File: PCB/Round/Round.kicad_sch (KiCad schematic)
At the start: 50 parts, among them J3 Conn, SW1 ESE13V01D, U1 PN532, U2 QR, Y1 27.12MHz

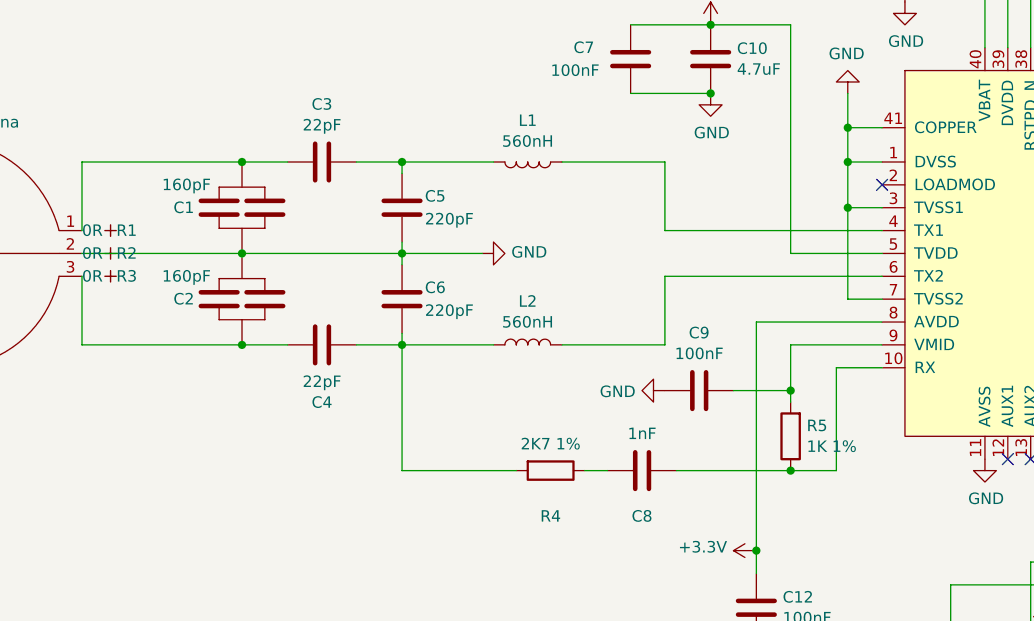
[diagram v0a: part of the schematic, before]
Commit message: Production nearly ready - may have to change to square LEDs.
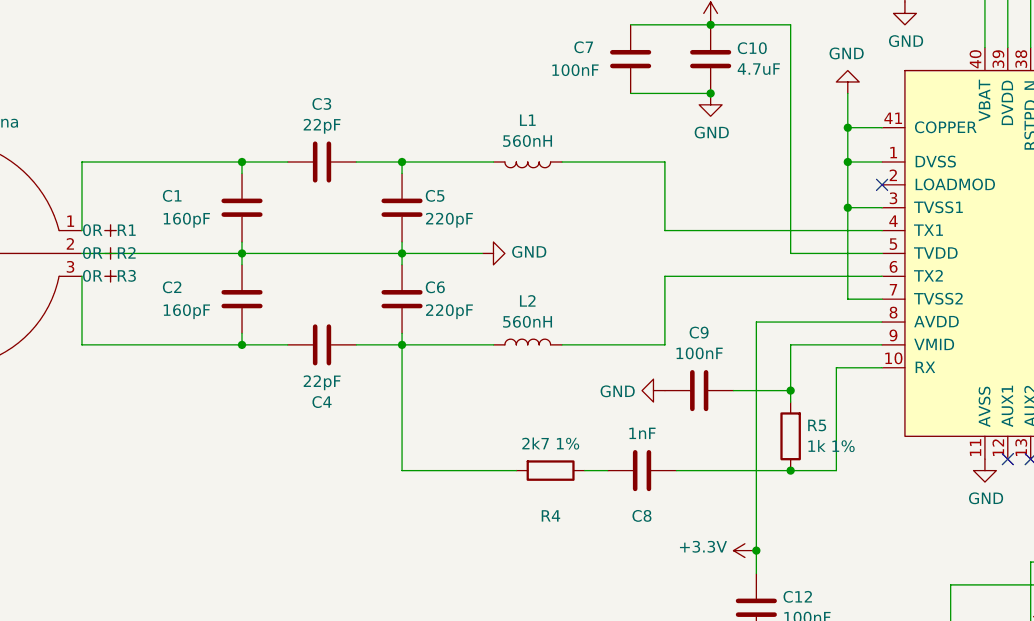
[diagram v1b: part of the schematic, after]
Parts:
- removed C1, C2: 160pF, RevK:C_0603, symbol RevK:Cx2
- added C1, C2: 160pF, RevK:C_0603, symbol Device:C
- D1: JLCPCB Rotation Offset (none) -> 180; LCSC Part # (none) -> C4749157
- D2: JLCPCB Rotation Offset (none) -> 180
- D3: JLCPCB Rotation Offset (none) -> 180; LCSC Part # (none) -> C2892757
- D4, D5, D6, U1: JLCPCB Rotation Offset (none) -> -90
- J3: JLCPCB Rotation Offset (none) -> 90; LCSC Part # (none) -> C780063
- L1, L2: footprint RevK:L_1206_1008 -> Inductor_SMD:L_1210_3225Metric; LCSC Part # (none) -> C318049
- R4: value 2K7 1% -> 2k7 1%; LCSC Part # (none) -> C114612
- R5: value 1K 1% -> 1k 1%; LCSC Part # (none) -> C22548
- Y1: JLCPCB Rotation Offset (none) -> 180; LCSC Part # (none) -> C70591
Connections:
- net GND: now also C1.2, C2.1
- net at A1.1, C3.2: now also C1.1
- net at A1.3, C4.1: now also C2.2

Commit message: production for LEDs as well
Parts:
- D1: footprint RevK:STP_156120xx7530 -> RevK:LED_1206_Rev_Square; JLCPCB Rotation Offset 180 -> (none); LCSC Part # C4749157 -> C157737
- D2: footprint RevK:STP_156120xx7530 -> RevK:LED_1206_Rev_Square; JLCPCB Rotation Offset 180 -> (none); LCSC Part # (none) -> C125108
- D3: footprint RevK:STP_156120xx7530 -> RevK:LED_1206_Rev_Square; JLCPCB Rotation Offset 180 -> (none); LCSC Part # C2892757 -> C125107
- L1, L2: footprint Inductor_SMD:L_1210_3225Metric -> Inductor_SMD:L_1008_2520Metric; LCSC Part # C318049 -> C75639
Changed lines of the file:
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@@
     (property "Reference" "L1" (id 0) (at 99.06 88.1126 90))
     (property "Value" "560nH" (id 1) (at 99.06 90.424 90))
-    (property "Footprint" "Inductor_SMD:L_1210_3225Metric" (id 2) (at 99.06 92.71 0)
+    (property "Footprint" "Inductor_SMD:L_1008_2520Metric" (id 2) (at 99.06 92.71 0)
       (effects (font (size 1.27 1.27)) hide)
     )
@@
       (effects (font (size 1.27 1.27)) hide)
     )
-    (property "LCSC Part #" "C318049" (id 7) (at 99.06 92.71 90)
+    (property "LCSC Part #" "C75639" (id 7) (at 99.06 92.71 90)
       (effects (font (size 1.27 1.27)) hide)
     )
@@
     (property "Reference" "L2" (id 0) (at 99.06 108.204 90))
     (property "Value" "560nH" (id 1) (at 99.06 110.5154 90))
-    (property "Footprint" "Inductor_SMD:L_1210_3225Metric" (id 2) (at 99.06 113.03 0)
+    (property "Footprint" "Inductor_SMD:L_1008_2520Metric" (id 2) (at 99.06 113.03 0)
       (effects (font (size 1.27 1.27)) hide)
     )
@@
       (effects (font (size 1.27 1.27)) hide)
     )
-    (property "LCSC Part #" "C318049" (id 7) (at 99.06 113.03 90)
+    (property "LCSC Part #" "C75639" (id 7) (at 99.06 113.03 90)
       (effects (font (size 1.27 1.27)) hide)
     )
@@
     (property "Reference" "D1" (id 0) (at 199.2122 24.9682 0))
     (property "Value" "G" (id 1) (at 199.2122 27.2796 0))
-    (property "Footprint" "RevK:STP_156120xx7530" (id 2) (at 199.39 30.48 0)
+    (property "Footprint" "RevK:LED_1206_Rev_Square" (id 2) (at 199.39 30.48 0)
       (effects (font (size 1.27 1.27)) hide)
     )
@@
       (effects (font (size 1.27 1.27)) hide)
     )
-    (property "LCSC Part #" "C4749157" (id 7) (at 199.39 30.48 0)
-      (effects (font (size 1.27 1.27)) hide)
-    )
-    (property "JLCPCB Rotation Offset" "180" (id 8) (at 199.39 30.48 0)
+    (property "LCSC Part #" "C157737" (id 7) (at 199.39 30.48 0)
       (effects (font (size 1.27 1.27)) hide)
     )
@@
     (property "Reference" "D2" (id 0) (at 199.2122 40.2082 0))
     (property "Value" "A" (id 1) (at 199.2122 42.5196 0))
-    (property "Footprint" "RevK:STP_156120xx7530" (id 2) (at 199.39 45.72 0)
+    (property "Footprint" "RevK:LED_1206_Rev_Square" (id 2) (at 199.39 45.72 0)
       (effects (font (size 1.27 1.27)) hide)
     )
@@
       (effects (font (size 1.27 1.27)) hide)
     )
-    (property "JLCPCB Rotation Offset" "180" (id 7) (at 199.39 45.72 0)
+    (property "LCSC Part #" "C125108" (id 8) (at 199.39 45.72 0)
       (effects (font (size 1.27 1.27)) hide)
     )
@@
     (property "Reference" "D3" (id 0) (at 199.2122 56.7182 0))
     (property "Value" "R" (id 1) (at 199.2122 59.0296 0))
-    (property "Footprint" "RevK:STP_156120xx7530" (id 2) (at 199.39 62.23 0)
-      (effects (font (size 1.27 1.27)) hide)
-    )
-    (property "Datasheet" "https://www.mouser.co.uk/ProductDetail/710-156120RS75300" (id 3) (at 199.39 62.23 0)
+    (property "Footprint" "RevK:LED_1206_Rev_Square" (id 2) (at 199.39 62.23 0)
+      (effects (font (size 1.27 1.27)) hide)
+    )
+    (property "Datasheet" "~" (id 3) (at 199.39 62.23 0)
       (effects (font (size 1.27 1.27)) hide)
     )
@@
       (effects (font (size 1.27 1.27)) hide)
     )
-    (property "LCSC Part #" "C2892757" (id 7) (at 199.39 62.23 0)
-      (effects (font (size 1.27 1.27)) hide)
-    )
-    (property "JLCPCB Rotation Offset" "180" (id 8) (at 199.39 62.23 0)
+    (property "LCSC Part #" "C125107" (id 7) (at 199.39 62.23 0)
       (effects (font (size 1.27 1.27)) hide)
     )
@@
     )
     (path "/00000000-0000-0000-0000-0000607e9287"
-      (reference "D1") (unit 1) (value "G") (footprint "RevK:STP_156120xx7530")
+      (reference "D1") (unit 1) (value "G") (footprint "RevK:LED_1206_Rev_Square")
     )
     (path "/00000000-0000-0000-0000-0000607eaf87"
-      (reference "D2") (unit 1) (value "A") (footprint "RevK:STP_156120xx7530")
+      (reference "D2") (unit 1) (value "A") (footprint "RevK:LED_1206_Rev_Square")
     )
     (path "/00000000-0000-0000-0000-0000607eb52d"
-      (reference "D3") (unit 1) (value "R") (footprint "RevK:STP_156120xx7530")
+      (reference "D3") (unit 1) (value "R") (footprint "RevK:LED_1206_Rev_Square")
     )
     (path "/00000000-0000-0000-0000-0000609ca448"
@@
     )
     (path "/00000000-0000-0000-0000-00006075bc21"
-      (reference "L1") (unit 1) (value "560nH") (footprint "Inductor_SMD:L_1210_3225Metric")
+      (reference "L1") (unit 1) (value "560nH") (footprint "Inductor_SMD:L_1008_2520Metric")
     )
     (path "/00000000-0000-0000-0000-00006075c317"
-      (reference "L2") (unit 1) (value "560nH") (footprint "Inductor_SMD:L_1210_3225Metric")
+      (reference "L2") (unit 1) (value "560nH") (footprint "Inductor_SMD:L_1008_2520Metric")
     )
     (path "/9d1ee0b7-8453-459c-a833-897b79b8b1c4"

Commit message: Panel
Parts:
- added PCB1: 70x70, RevK:PCB7070, symbol RevK:PCB
- added V1, V2, V3, V4: ~, RevK:VCUT70, symbol RevK:VCUT

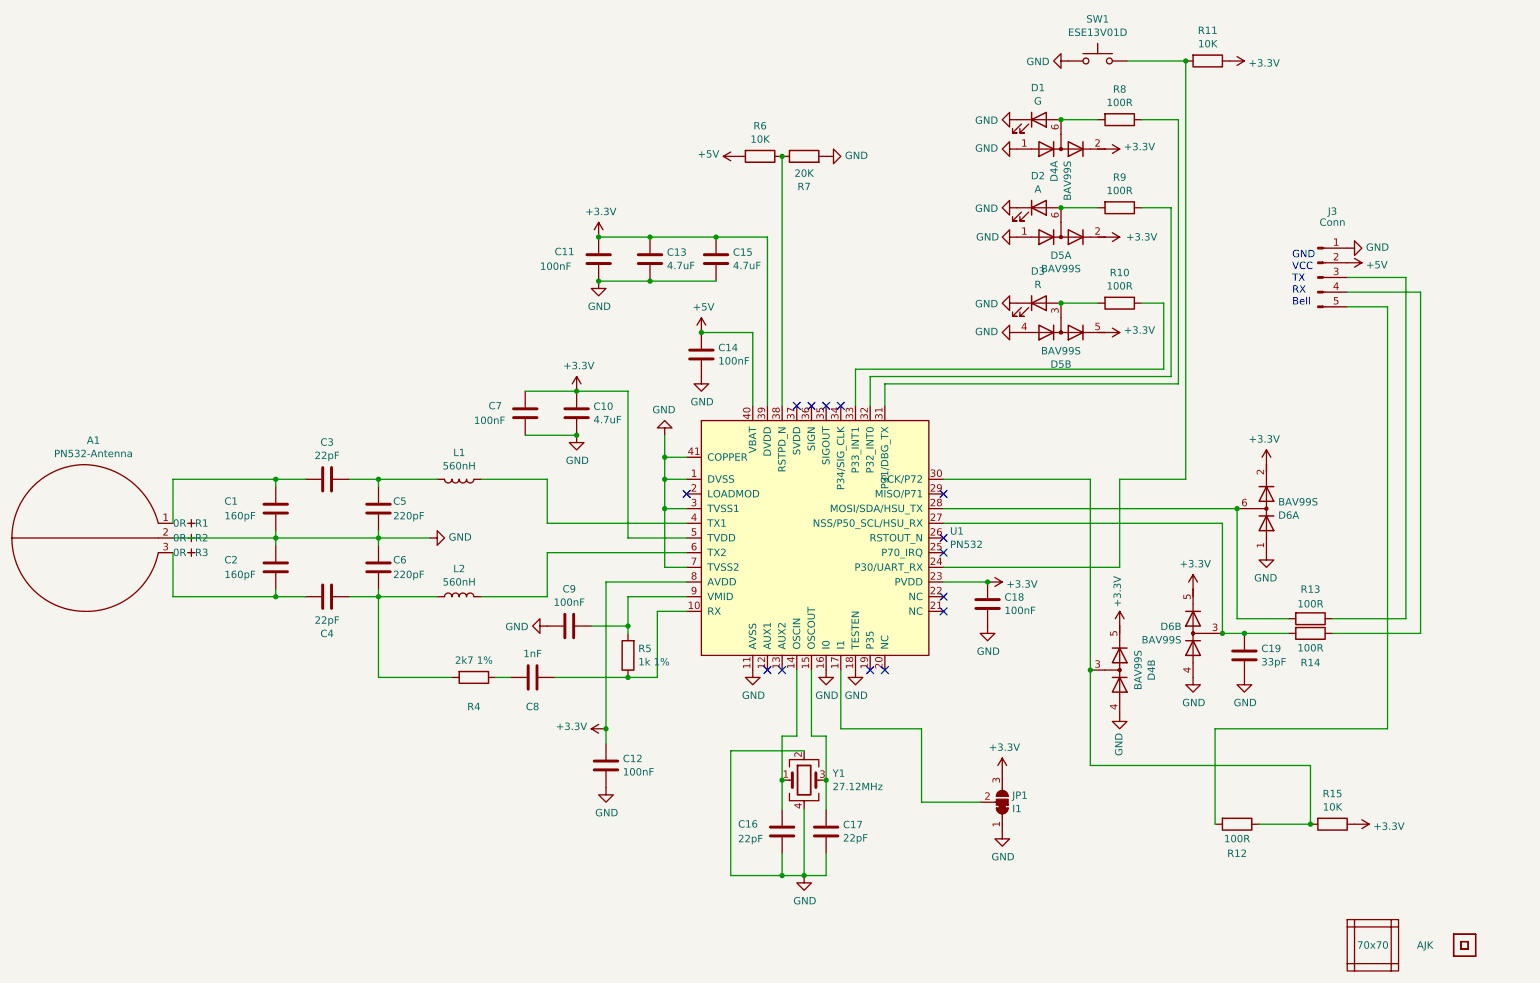
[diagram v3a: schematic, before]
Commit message: Tidy and new ESP diodes
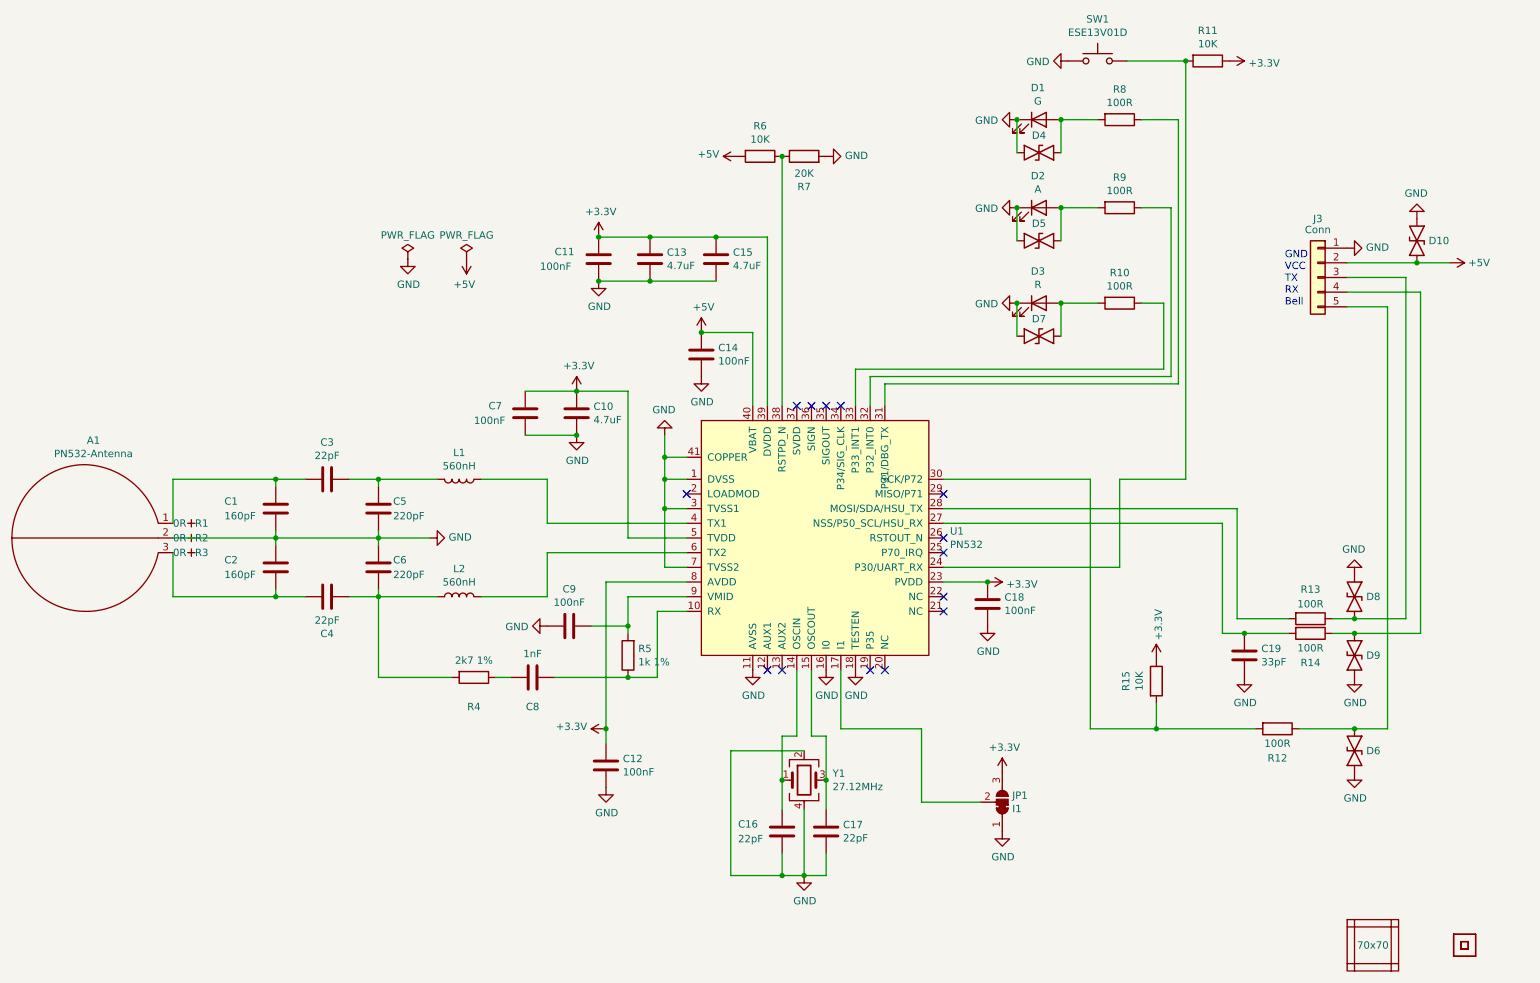
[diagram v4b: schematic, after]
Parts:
- removed D4, D5, D6: BAV99S, RevK:SOT-363_SC-70-6, symbol Diode:BAV99S
- added D10, D4, D5, D6, D7, D8, D9: ~, RevK:DFN1006-2L, symbol RevK:ES05D1MC10
- J3: symbol Connector:Conn_01x05_Male -> Connector_Generic:Conn_01x05
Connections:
- net +5V: now also D10.2
- net GND: now also D10.1, D4.2, D5.2, D6.2, D7.2, D8.1, D9.2
- net at R15.2, U1.30 (SCK/P72): now also R12.2; no longer R12.1
- net at J3.3 (Pin_3), R13.1: now also D8.2
- net at J3.4 (Pin_4), R14.1: now also D9.1
- net at J3.5 (Pin_5): now also R12.1, D6.1; no longer R12.2
- net at D1.2 (A), R8.2: now also D4.1
- net at D2.2 (A), R9.2: now also D5.1
- net at D3.2 (A), R10.2: now also D7.1
- net +3V3 renamed +3.3V
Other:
- moved on the sheet: R12, R15

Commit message: Tidy
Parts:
- removed AJK1: AJK, RevK:AJK, symbol RevK:AJK
- added C20: 100uF 6.3V, RevK:C_1206, symbol Device:C
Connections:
- net +5V: now also C20.2
- net GND: now also C20.1
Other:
- moved on the sheet: C11, C13, C14, C15
